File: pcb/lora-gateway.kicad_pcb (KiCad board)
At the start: 2 copper layers, 70.8 x 25.8 mm, 6 parts, among them J1 USB_B_Micro, J2 Conn_01x06, J3 Conn_01x06, J4 Conn_Coaxial, U1 RFM95W-868S2, U2 ATmega2560-16A

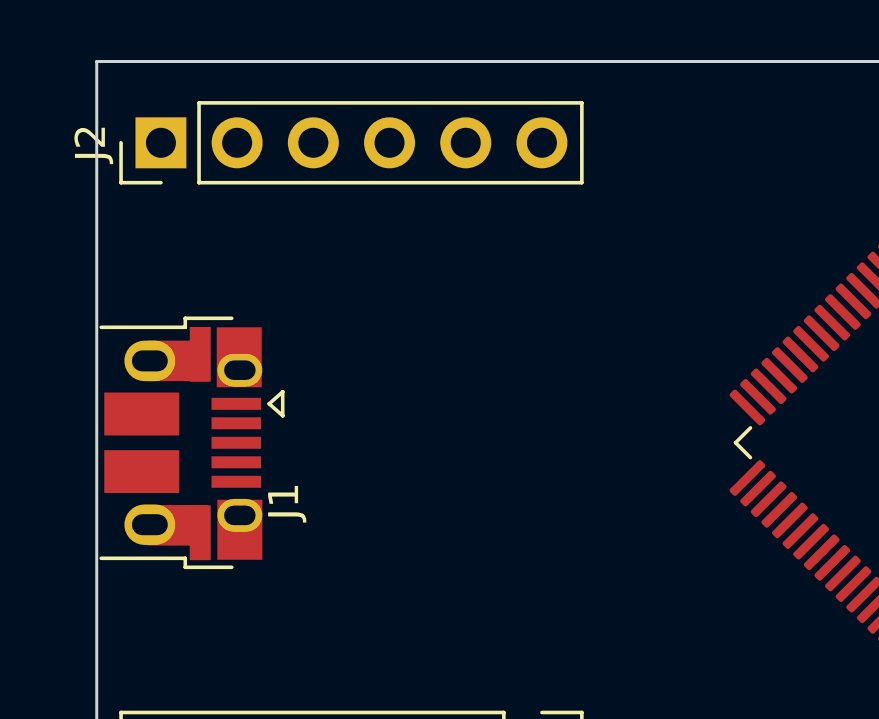
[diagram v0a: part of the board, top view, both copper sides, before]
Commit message: add regulator
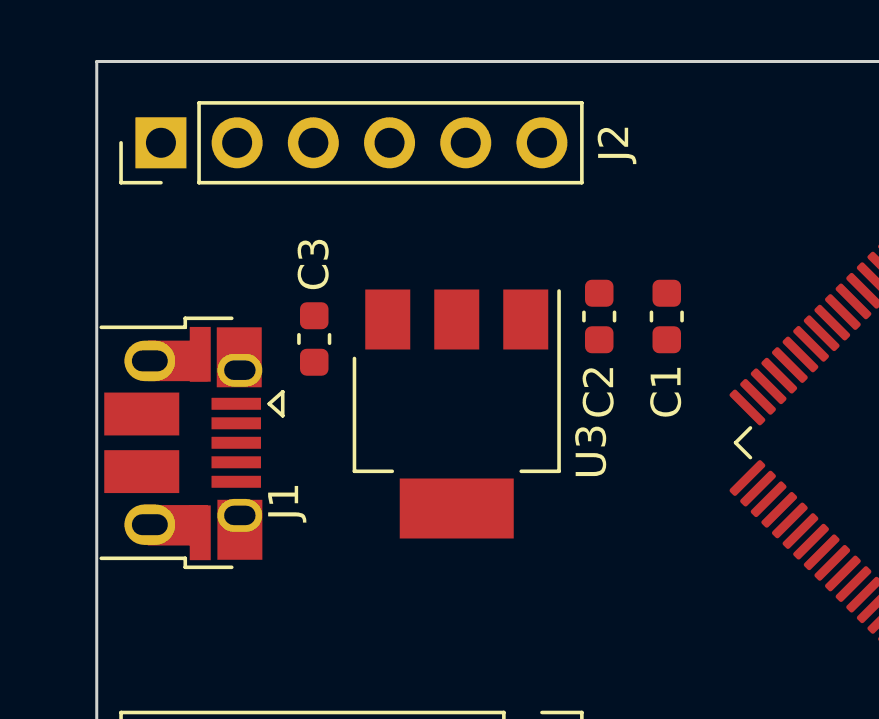
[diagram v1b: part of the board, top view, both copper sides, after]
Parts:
- added C1: C_Small, Capacitor_SMD:C_0603_1608Metric, F.Cu at (57.5, 66.8)
- added C2: C_Small, Capacitor_SMD:C_0603_1608Metric, F.Cu at (55.2, 66.8)
- added C3: C_Small, Capacitor_SMD:C_0603_1608Metric, F.Cu at (45.8, 67.5)
- added U3: LM1117-3.3, Package_TO_SOT_SMD:SOT-223-3_TabPin2, F.Cu at (50.5, 70.0)

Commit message: pcb wiring
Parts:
- added C4: C_Small, Capacitor_SMD:C_0603_1608Metric, F.Cu at (111.7, 68.4)
- added C5: C_Small, Capacitor_SMD:C_0603_1608Metric, F.Cu at (64.1, 81.0)
- added C6: C_Small, Capacitor_SMD:C_0603_1608Metric, F.Cu at (58.3, 75.3)
- added J5: AVR-JTAG-10, Connector_PinHeader_2.54mm:PinHeader_2x05_P2.54mm_Vertical, F.Cu at (86.4, 65.3)
- added J6: AVR-ISP-6, Connector_PinHeader_2.54mm:PinHeader_2x03_P2.54mm_Vertical, F.Cu at (57.8, 63.1)
- added R1: R_Small, Resistor_SMD:R_0603_1608Metric, F.Cu at (55.0, 72.9)
- added SW1: SW_Push, Button_Switch_SMD:SW_SPST_CK_RS282G05A3, F.Cu at (50.8, 76.9)
- added Y1: Crystal, Crystal:Crystal_SMD_5032-2Pin_5.0x3.2mm, F.Cu at (61.8, 77.6)
- moved U1 8.41 mm to (100.9, 70.2)
- moved J4 7.59 mm to (114.6, 77.2)
- moved U2 1.91 mm to (71.8, 71.1)
- moved C1 0.46 mm to (57.0, 66.7)
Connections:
- U2 pad 10: Net-(U2-VCC-Pad10) -> +3V3
- U2 pad 100: unconnected-(U2-AVCC-Pad100) -> +3V3
- U2 pad 30: unconnected-(U2-~{RESET}-Pad30) -> RST
- U2 pad 31: Net-(U2-VCC-Pad10) -> +3V3
- U2 pad 33: unconnected-(U2-XTAL2-Pad33) -> Net-(U2-XTAL2)
- U2 pad 34: unconnected-(U2-XTAL1-Pad34) -> Net-(U2-XTAL1)
- U2 pad 61: Net-(U2-VCC-Pad10) -> +3V3
- U2 pad 80: Net-(U2-VCC-Pad10) -> +3V3
- U2 pad 90: unconnected-(U2-PF7-Pad90) -> TDI
- U2 pad 91: unconnected-(U2-PF6-Pad91) -> TDO
- U2 pad 92: unconnected-(U2-PF5-Pad92) -> TMS
- U2 pad 93: unconnected-(U2-PF4-Pad93) -> TCK
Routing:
- net +3V3: track 0.00 -> 128.8 mm, vias 0 -> 2
- net +5V: track 0.00 -> 81.3 mm, vias 0 -> 1
- net RST: track 0.00 -> 75.8 mm, vias 0 -> 3
- net MISO: track 0.00 -> 74.3 mm, vias 0 -> 4
- net MOSI: track 0.00 -> 71.5 mm, vias 0 -> 3
- net SCK: track 0.00 -> 67.3 mm, vias 0 -> 1
- net SS_LORA: track 0.00 -> 56.9 mm, vias 0 -> 2
- net SS_ETH: track 0.00 -> 29.7 mm
- net TDO: track 0.00 -> 19.5 mm
- net TDI: track 0.00 -> 17.2 mm
- net TMS: track 0.00 -> 14.5 mm
- net TCK: track 0.00 -> 12.8 mm
- net GND: track 0.00 -> 9.80 mm, vias 0 -> 24
- net unconnected-(J1-Shield-Pad6): track 0.00 -> 8.75 mm
- net Net-(U2-XTAL2): track 0.00 -> 7.03 mm
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- added copper zone on B.Cu, net GND
- added copper zone on F.Cu, net GND
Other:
- board size 70.8 x 25.8 mm -> 78.3 x 25.8 mm
